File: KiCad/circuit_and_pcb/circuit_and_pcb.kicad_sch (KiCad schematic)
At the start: 1 part

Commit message: finish motor diagram
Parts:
- added ALEFT: Motor_Controller_Left, Module:Pololu_Breakout-16_15.2x20.3mm, symbol Driver_Motor:Pololu_Breakout_A4988
- added ARIGHT: Motor_Controller_Right, Module:Pololu_Breakout-16_15.2x20.3mm, symbol Driver_Motor:Pololu_Breakout_A4988
- added J1: Barrel_Jack, symbol Connector:Barrel_Jack
- added MLEFT: Stepper_Motor_Left, symbol Motor:Stepper_Motor_bipolar
- added MRIGHT: Stepper_Motor_Right, symbol Motor:Stepper_Motor_bipolar
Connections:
- net at A?.19 (D4): now also ALEFT.16 (DIR)
- net at A?.20 (D5): now also ALEFT.15 (STEP)
- net at A?.21 (D6): now also ALEFT.9 (~{ENABLE})
- net at A?.23 (D8): now also ARIGHT.16 (DIR)
- net at A?.24 (D9): now also ARIGHT.15 (STEP)
- net at A?.25 (D10): now also ARIGHT.9 (~{ENABLE})
- net at A?.5 (+5V): now also ALEFT.2 (VDD), ARIGHT.2 (VDD)
- net at A?.7 (GND): now also ALEFT.1 (GND), ARIGHT.1 (GND)
- new net: ARIGHT.5 (2A), MRIGHT.1
- new net: ARIGHT.4 (1A), MRIGHT.2 (-)
- new net: ARIGHT.3 (1B), MRIGHT.3
- new net: ARIGHT.6 (2B), MRIGHT.4
- new net: ALEFT.5 (2A), MLEFT.1
- new net: ALEFT.4 (1A), MLEFT.2 (-)
- new net: ALEFT.3 (1B), MLEFT.3
- new net: ALEFT.6 (2B), MLEFT.4
- new net: ALEFT.7 (GND), ARIGHT.7 (GND), J1.2
- new net: ALEFT.8 (VMOT), ARIGHT.8 (VMOT), J1.1
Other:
- company: (none) -> FW
- title: (none) -> Automatic Chess Motor Diagram
- moved on the sheet: A?

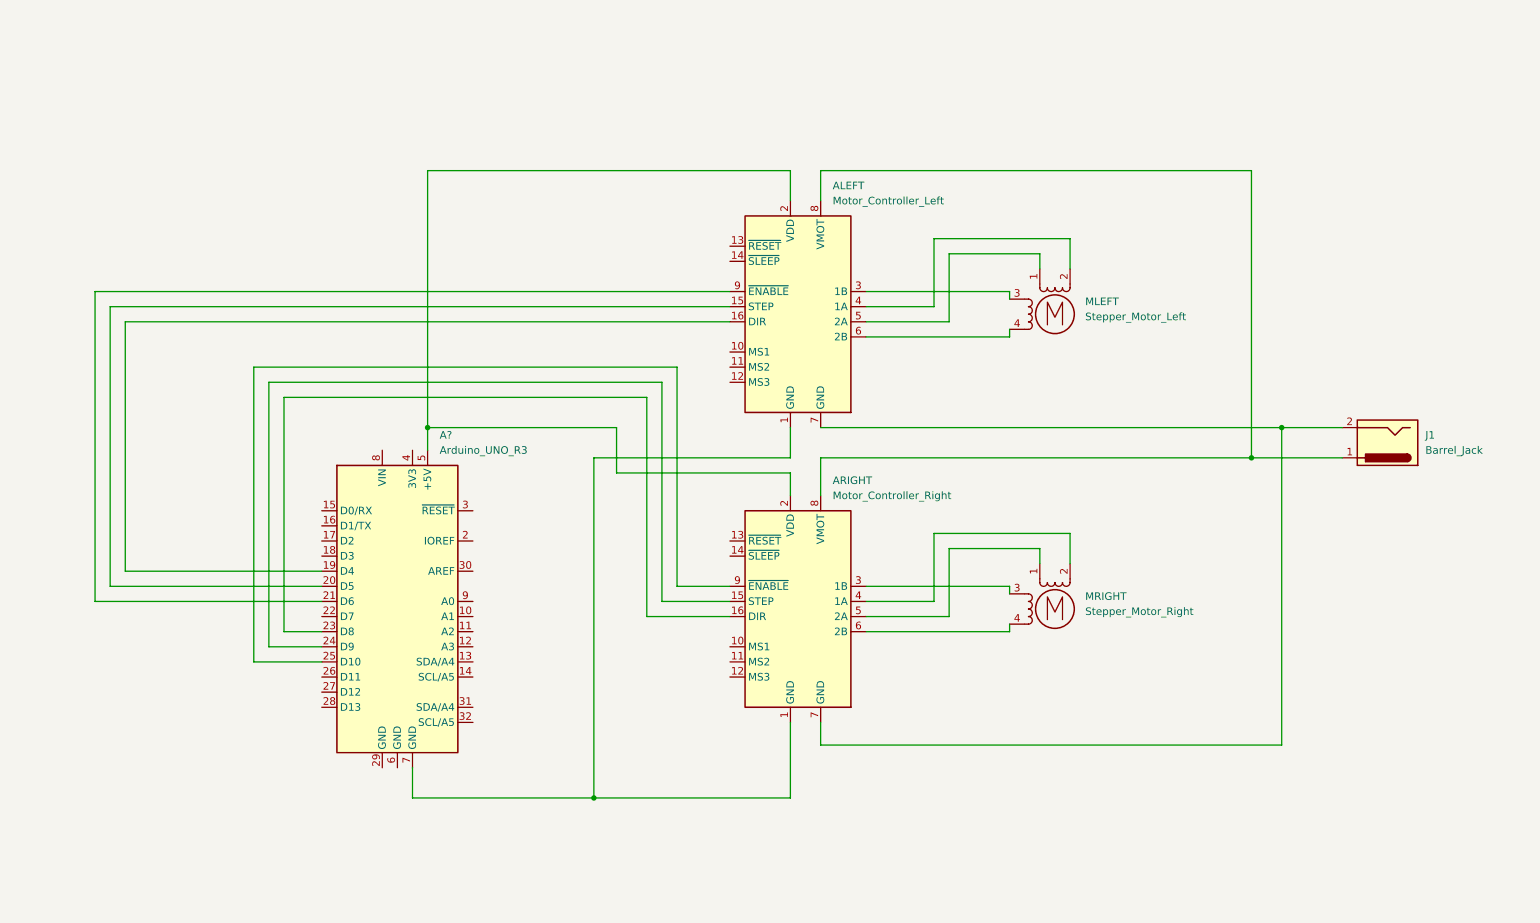
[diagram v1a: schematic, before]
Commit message: extend circuit diagram
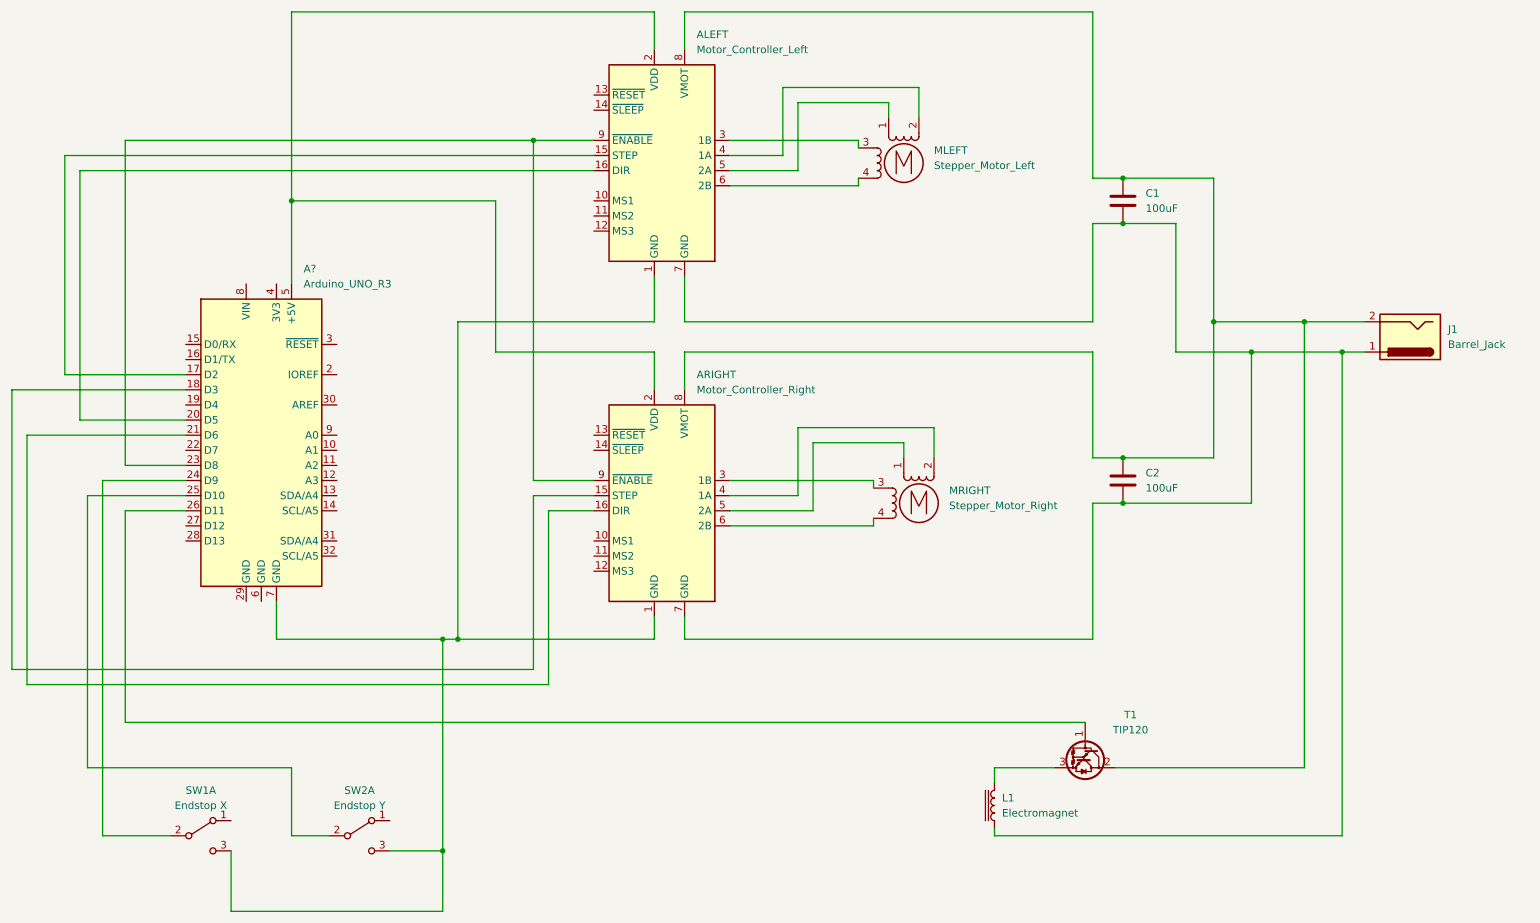
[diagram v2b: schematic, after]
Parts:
- added C1, C2: 100uF, symbol Device:C
- added L1: Electromagnet, symbol Device:L_Iron
- added SW1: Endstop X, symbol Switch:SW_DPDT_x2
- added SW2: Endstop Y, symbol Switch:SW_DPDT_x2
- added T1: TIP120, Package_TO_SOT_THT:TO-220-3_Vertical, symbol Transistor_BJT:TIP120
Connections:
- net at A?.17 (D2): now also ALEFT.15 (STEP)
- net at A?.18 (D3): now also ARIGHT.15 (STEP)
- net at A?.19 (D4): no longer ALEFT.16 (DIR)
- net at A?.20 (D5): now also ALEFT.16 (DIR); no longer ALEFT.15 (STEP)
- net at A?.21 (D6): now also ARIGHT.16 (DIR); no longer ALEFT.9 (~{ENABLE})
- net at A?.23 (D8): now also ALEFT.9 (~{ENABLE}), ARIGHT.9 (~{ENABLE}); no longer ARIGHT.16 (DIR)
- net at A?.24 (D9): now also SW1.2 (B); no longer ARIGHT.15 (STEP)
- net at A?.25 (D10): now also SW2.2 (B); no longer ARIGHT.9 (~{ENABLE})
- net at A?.26 (D11): now also T1.1 (B)
- net at A?.7 (GND), ALEFT.1 (GND), ARIGHT.1 (GND): now also SW1.3 (C), SW2.3 (C)
- net at ALEFT.7 (GND), ARIGHT.7 (GND): now also J1.1, C1.1, C2.1, L1.1; no longer J1.2
- net at ALEFT.8 (VMOT), ARIGHT.8 (VMOT): now also J1.2, C1.2, C2.2, T1.2 (C); no longer J1.1
- new net: L1.2, T1.3 (E)
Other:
- title: Automatic Chess Motor Diagram -> Automatic Chess Diagram
- moved on the sheet: A?, ALEFT, ARIGHT, J1, MLEFT, MRIGHT
